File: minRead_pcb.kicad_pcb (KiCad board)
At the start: 2 copper layers, 62.4 x 117.6 mm, 119 parts, among them J1 USB_C_Receptacle, J2 FH34SRJ-24S-0.5SH_50_, J3 FH34SRJ-6S-0.5SH_50_, J5 Conn_01x02, J7 Micro_SD_Card, Q10 BSS138, Q11 BSS138, Q16 MMBT3906, Q17 MMBT3904, Q18 AO3419, Q4 [BSS138] AO3400A, Q5 AO3419, Q6 AO3419, SW1 SW_Push, SW10 SW_Push, SW11 SW_Push, SW2 SW_Push, SW3 SW_Push, SW4 SW_Push, SW6 SW_Push, SW8 SW_Push, SW9 SW_Push, U1 TPD4E1U06DBVR, U11 AP3031KTR, U3 AP2112K-3.3, U4 ESP32-S3-WROOM-1, U6 TPD4E1U06DBVR, U7 MCP73832-2-OT

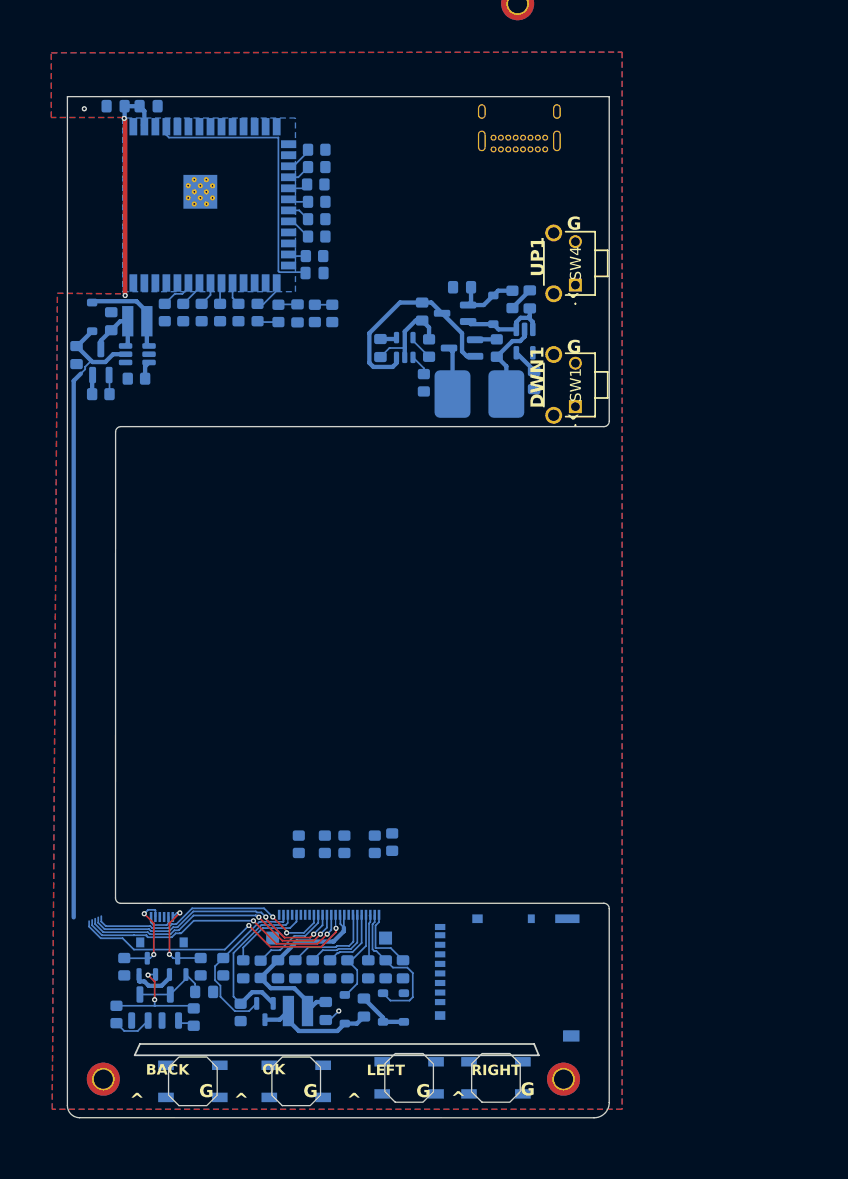
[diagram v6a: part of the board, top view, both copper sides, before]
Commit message: proper port positioning
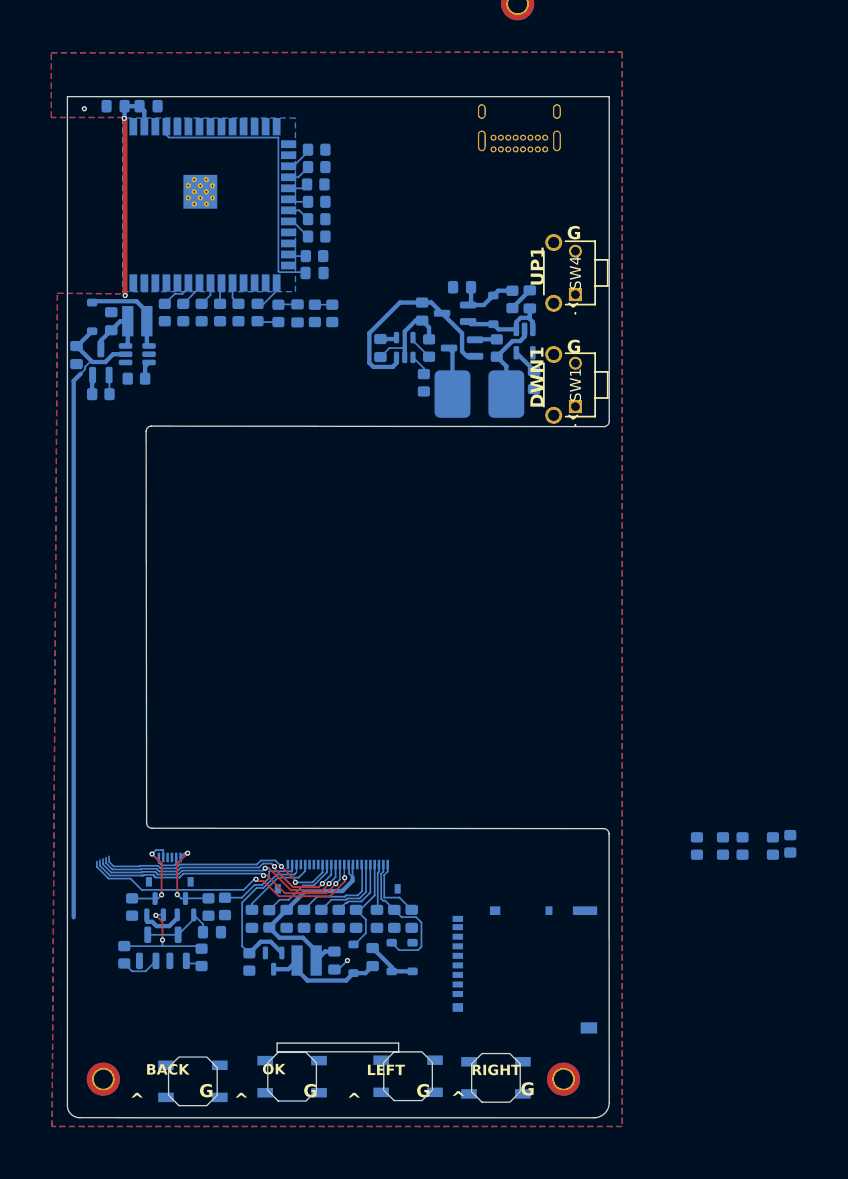
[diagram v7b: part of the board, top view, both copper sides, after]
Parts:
- moved R4 45.9 mm to (126.6, 118.2)
- moved R53 45.9 mm to (124.6, 118.4)
- moved R54 45.9 mm to (121.1, 118.4)
- moved R55 45.9 mm to (118.8, 118.4)
- moved R8 45.9 mm to (115.8, 118.4)
- moved R15 6.95 mm to (61.5, 125.3)
- moved R62 6.93 mm to (59.6, 125.4)
- moved R63 6.93 mm to (50.8, 125.4)
- moved C30 6.93 mm to (60.0, 128.3)
- moved J3 6.93 mm to (55.1, 121.1)
- moved Q16 6.93 mm to (56.1, 130.1)
- moved Q17 6.93 mm to (52.6, 130.1)
- moved R47 6.93 mm to (58.8, 131.2)
- moved R48 6.93 mm to (49.9, 130.9)
- moved Q10 6.93 mm to (57.0, 125.4)
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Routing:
- net /GDR: track 21.5 -> 11.9 mm
- net EPD_MOSI: track 35.0 -> 34.4 mm
- net EPD_BUSY: track 29.1 -> 28.5 mm
- net EPD_DC: track 31.0 -> 30.4 mm
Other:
- outline, holes or cut-outs redrawn
